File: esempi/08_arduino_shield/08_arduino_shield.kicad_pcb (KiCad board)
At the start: 2 copper layers, 7 parts, among them J1 Arduino_Header, P1 CONN_01X02, U1 ULN2803

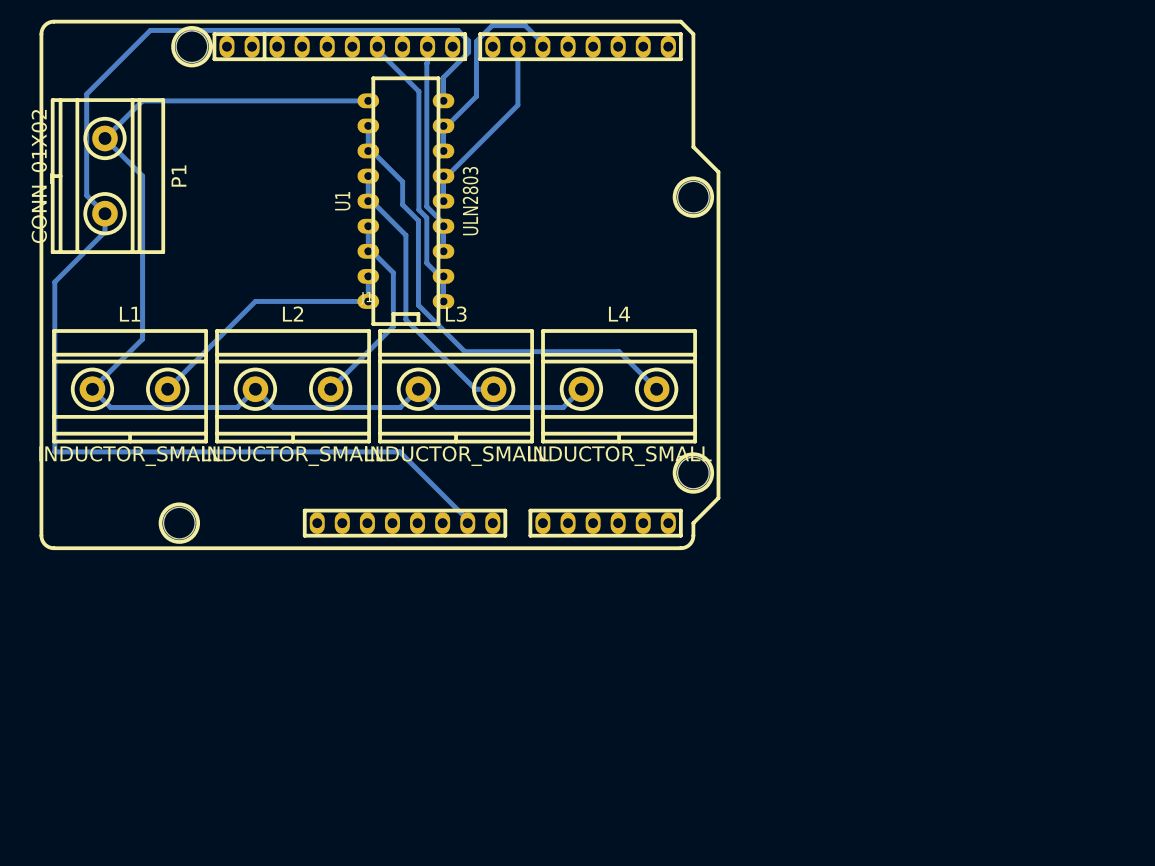
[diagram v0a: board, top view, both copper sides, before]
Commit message: Modifiche ad arduino shield per connettori più piccoli
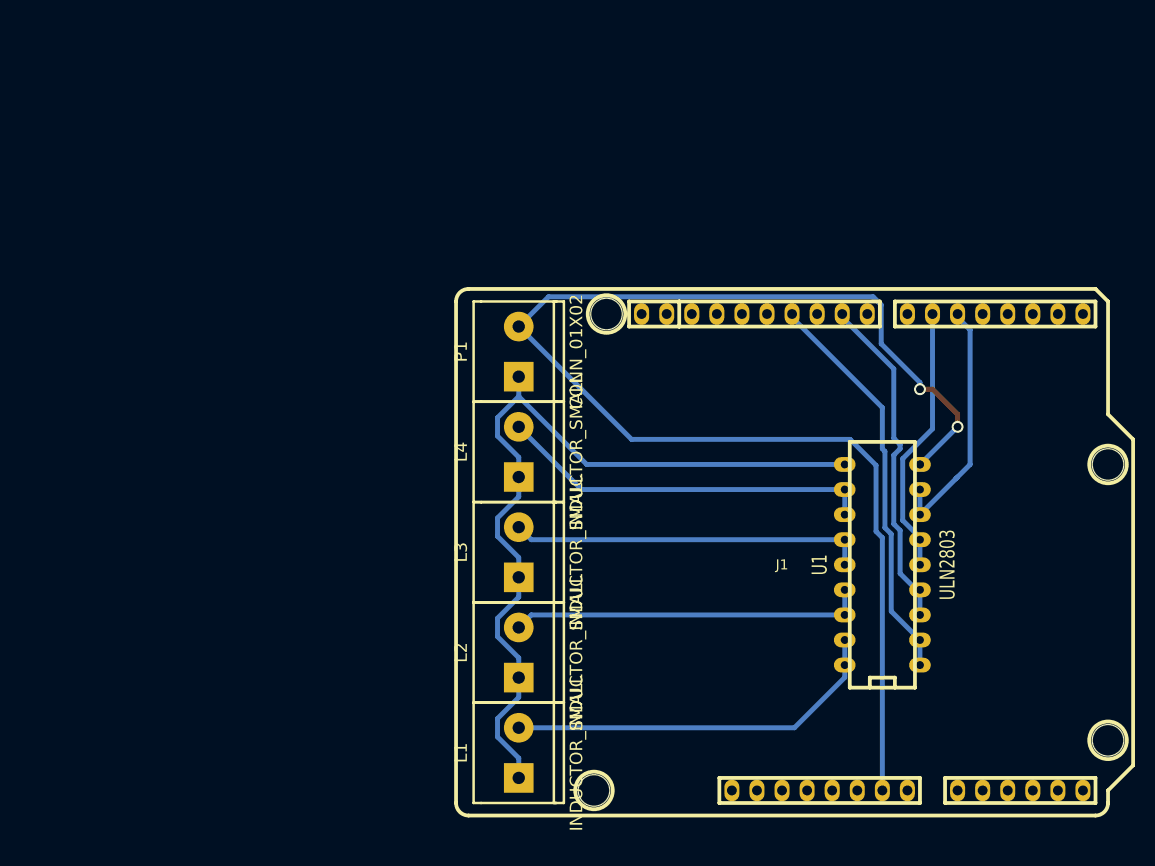
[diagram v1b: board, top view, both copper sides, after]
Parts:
- L1, L2, L3, L4, P1: footprint w_conn_gmkds:gmkds_3-2-7,62 -> w_conn_screw:mors_2p
- moved U1 60.7 mm to (200.7, 133.3)
- moved L1 53.9 mm to (163.8, 152.4), turned to 90 degrees
- moved J1 50.0 mm to (190.5, 132.1)
- moved P1 45.5 mm to (163.8, 111.8), turned to 90 degrees
- moved L2 35.1 mm to (163.8, 142.2), turned to 90 degrees
- moved L3 17.7 mm to (163.8, 132.1), turned to 90 degrees
- moved L4 12.0 mm to (163.8, 121.9), turned to 90 degrees
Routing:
- net VCC: track 111.5 -> 83.6 mm
- net Net-(L2-Pad2): track 20.4 -> 36.1 mm
- net Net-(J1-Pad24): track 21.5 -> 34.5 mm
- net Net-(L1-Pad2): track 26.5 -> 38.9 mm
- net Net-(J1-Pad26): track 28.8 -> 40.9 mm
- net Net-(L4-Pad2): track 48.1 -> 38.2 mm
- net Net-(J1-Pad21): track 19.0 -> 27.4 mm
- net Net-(L3-Pad2): track 28.1 -> 36.1 mm
- net Net-(J1-Pad20): track 21.2 -> 25.7 mm
- net GND: track 133.0 -> 135.6 mm, vias 0 -> 3
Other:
- net class Default: clearance 0.3 -> 0.4
- rule pad_to_mask_clearance: 0 -> 0.2
- rule trace_clearance: 0.3 -> 0.4
